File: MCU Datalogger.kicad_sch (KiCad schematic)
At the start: 25 parts, among them U1 24LC1025, U2 24LC1025, U3 DS1337S_, U4 ATMEGA328P-AU, Y1 16 MHz, Y2 32.768 KHz

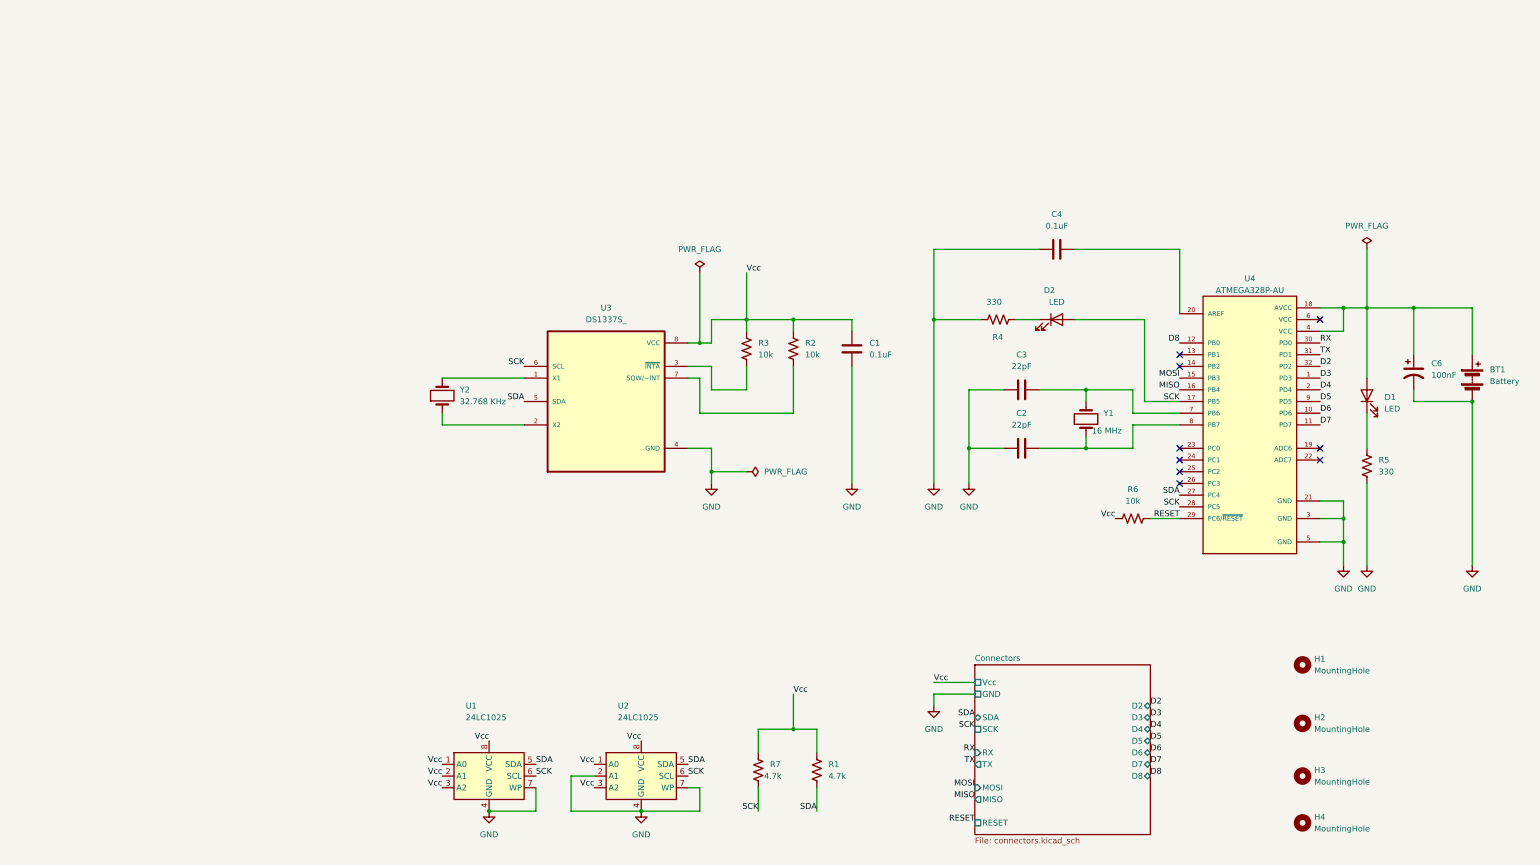
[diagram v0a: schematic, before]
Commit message: Completed comments and organization in schematic.
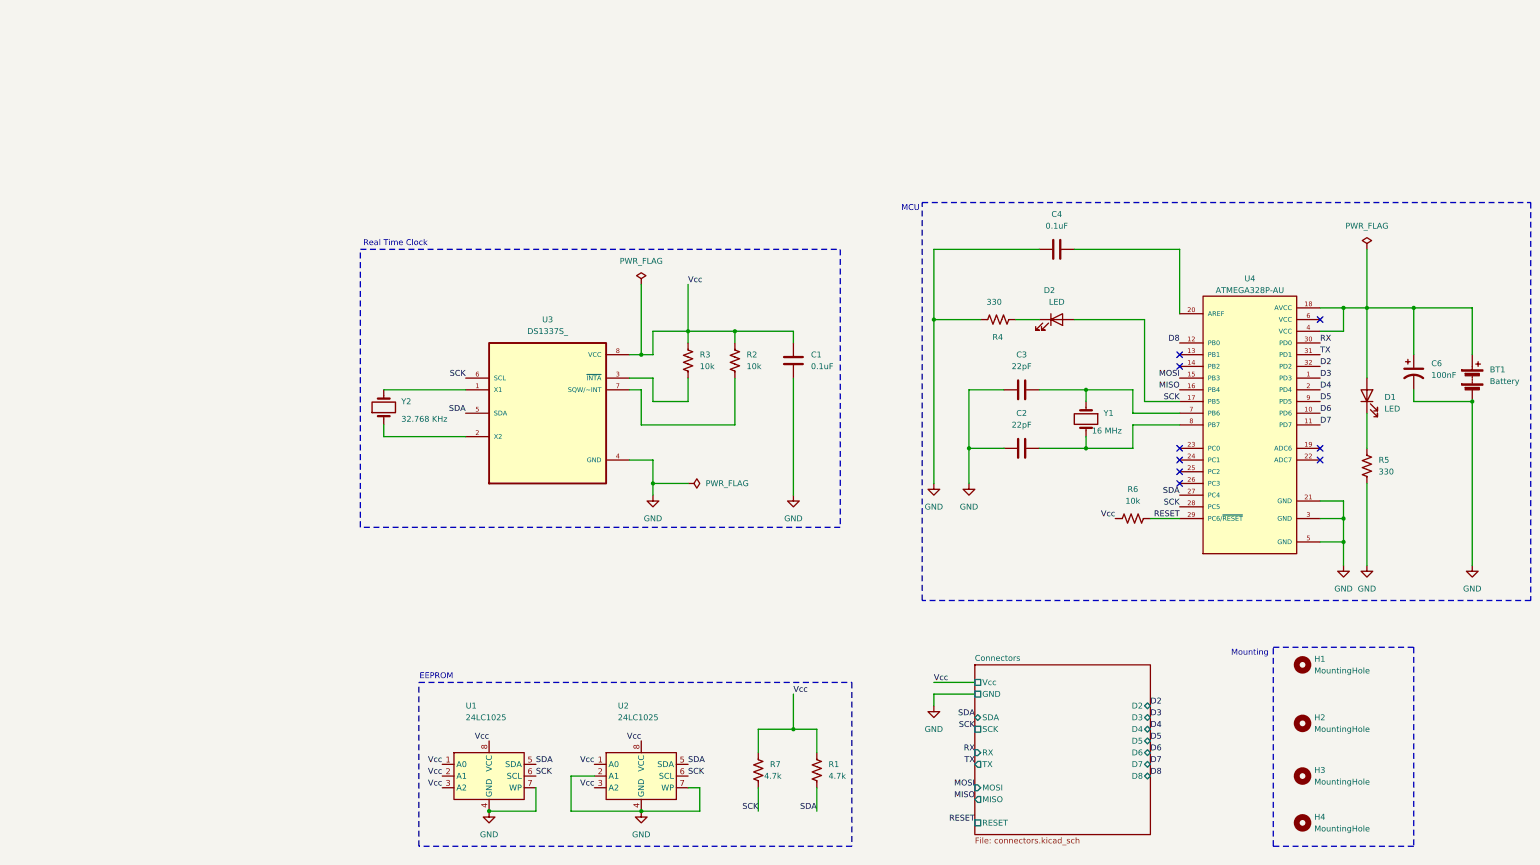
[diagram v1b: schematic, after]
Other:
- note added: "EEPROM"
- note added: "MCU"
- note added: "Mounting"
- note added: "Real Time Clock"
- moved on the sheet: C1, R2, R3, U3, Y2

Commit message: Fixed outstanding issues and set Silkscreen.
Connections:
- net Vcc: now also BT1.1 (+), C6.1, D1.2 (A), U4.18 (AVCC), U4.4 (VCC)
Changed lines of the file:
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@@
 	(wire
 		(pts
-			(xy 243.84 25.4) (xy 243.84 38.1)
-		)
-		(stroke
-			(width 0)
-			(type default)
-		)
-	)
-	(wire
-		(pts
 			(xy 106.68 43.18) (xy 106.68 45.72)
 		)
@@
 		)
 	)
+	(label "Vcc"
+		(at 243.84 38.1 0)
+		(fields_autoplaced yes)
+		(effects
+			(font
+				(size 1.27 1.27)
+			)
+			(justify left bottom)
+		)
+	)
 	(label "SDA"
 		(at 158.75 127 180)
@@
 					(unit 1)
 				)
-			)
-		)
-	)
-	(symbol
-		(lib_id "power:PWR_FLAG")
-		(at 243.84 25.4 0)
-		(unit 1)
-		(exclude_from_sim no)
-		(in_bom yes)
-		(on_board yes)
-		(dnp no)
-		(fields_autoplaced yes)
-		(property "Reference" "#FLG01"
-			(at 243.84 23.495 0)
-			(effects
-				(font
-					(size 1.27 1.27)
-				)
-				(hide yes)
-			)
-		)
-		(property "Value" "PWR_FLAG"
-			(at 243.84 20.32 0)
-			(effects
-				(font
-					(size 1.27 1.27)
-				)
-			)
-		)
-		(property "Footprint" ""
-			(at 243.84 25.4 0)
-			(effects
-				(font
-					(size 1.27 1.27)
-				)
-				(hide yes)
-			)
-		)
-		(property "Datasheet" "~"
-			(at 243.84 25.4 0)
-			(effects
-				(font
-					(size 1.27 1.27)
-				)
-				(hide yes)
-			)
-		)
-		(property "Description" "Special symbol for telling ERC where power comes from"
-			(at 243.84 25.4 0)
-			(effects
-				(font
-					(size 1.27 1.27)
-				)
-				(hide yes)
-			)
-		)
-		(pin "1"
-		)
-		(instances
-			(project ""
-				(path "/9701ff14-9a8f-43ab-a327-0923973e2750"
-					(reference "#FLG01")
-					(unit 1)
-				)

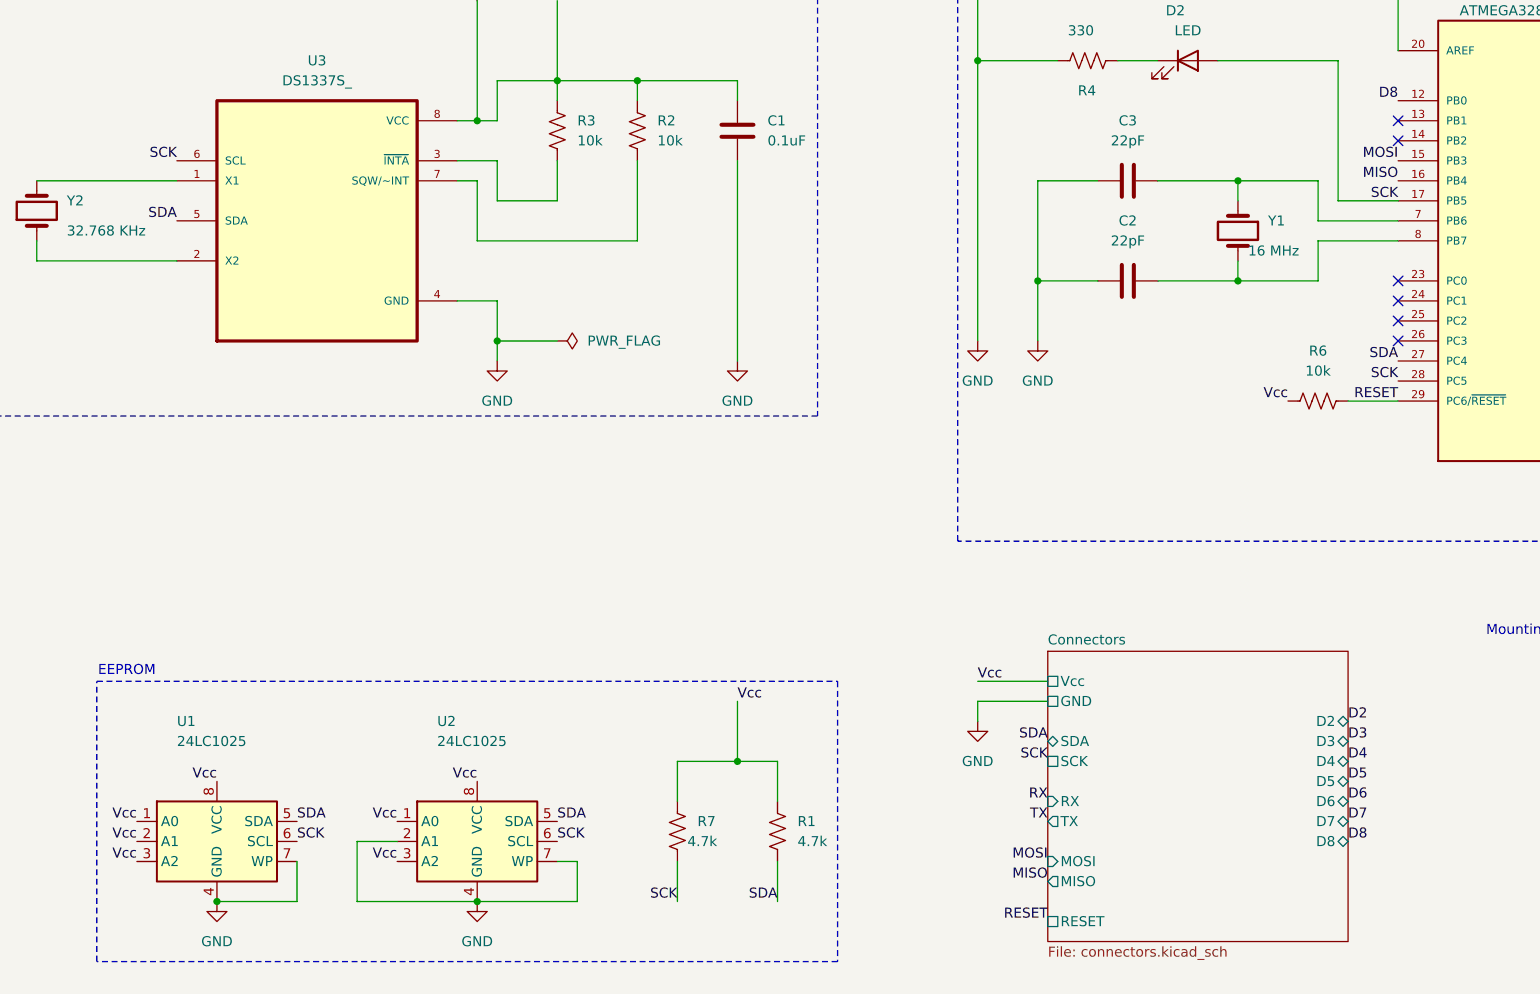
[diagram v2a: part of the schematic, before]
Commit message: Fixed defects relating to SCL/SCK confusion.
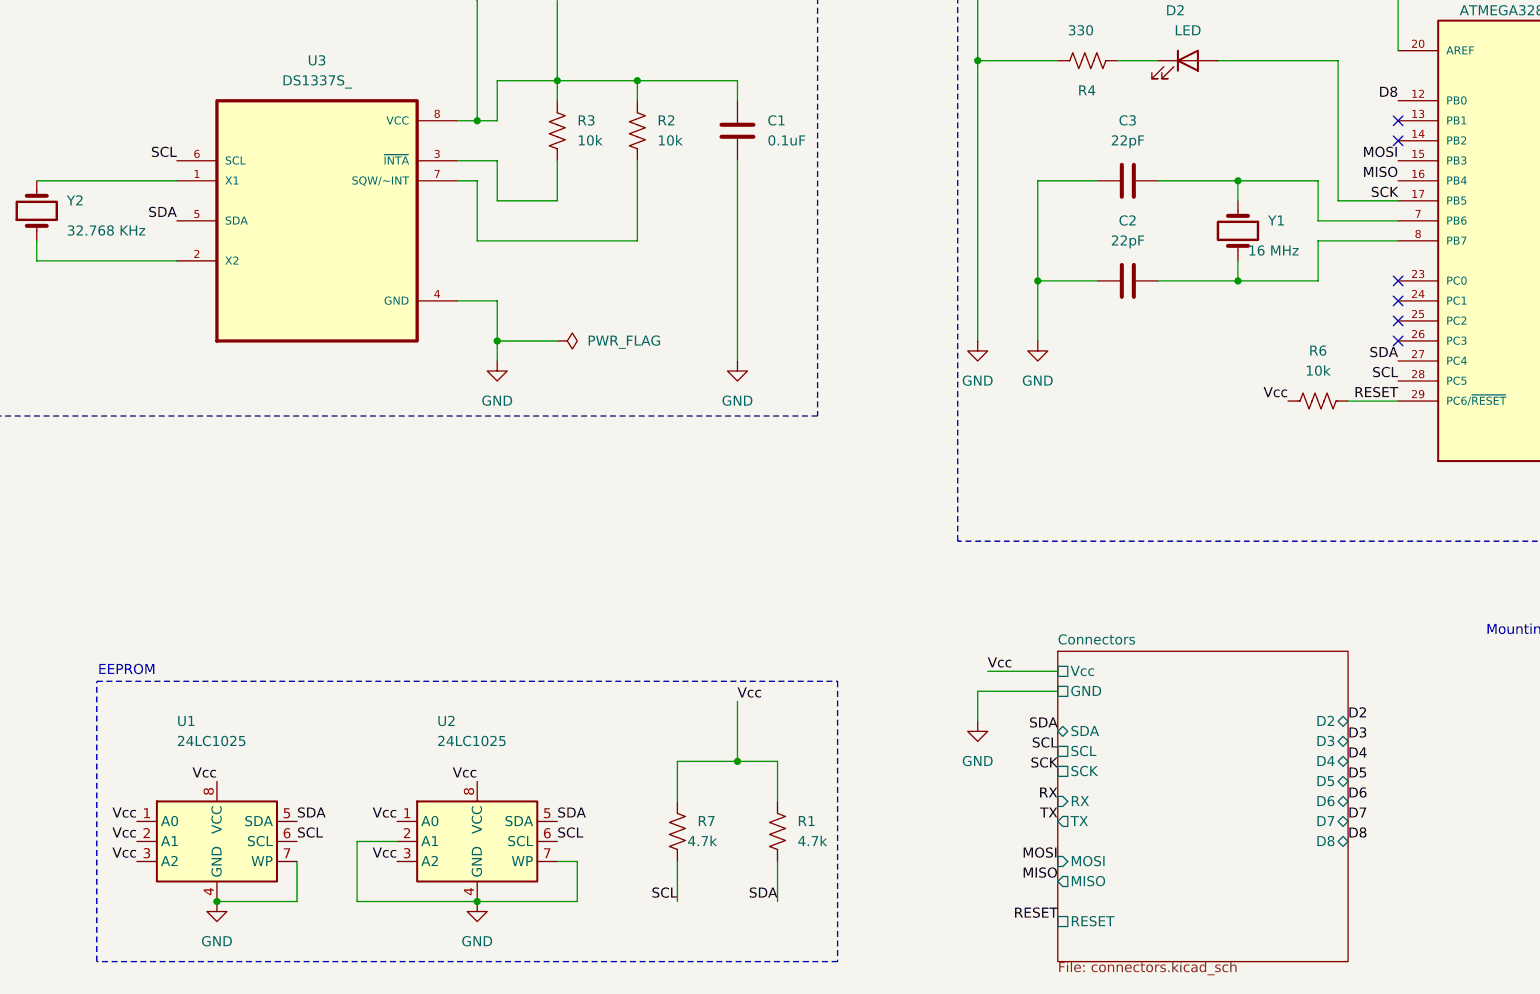
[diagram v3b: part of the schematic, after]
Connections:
- net SCK: no longer R7.1, U1.6 (SCL), U2.6 (SCL), U3.6 (SCL), U4.28 (PC5)
- new net SCL: R7.1, U1.6 (SCL), U2.6 (SCL), U3.6 (SCL), U4.28 (PC5)
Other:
- sheet Connectors ports: added SCL; removed none
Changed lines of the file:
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@@
 	(wire
 		(pts
+			(xy 149.86 120.65) (xy 160.02 120.65)
+		)
+		(stroke
+			(width 0)
+			(type default)
+		)
+	)
+	(wire
+		(pts
 			(xy 254 55.88) (xy 254 58.42)
 		)
@@
 	(wire
 		(pts
-			(xy 149.86 119.38) (xy 158.75 119.38)
-		)
-		(stroke
-			(width 0)
-			(type default)
-		)
-	)
-	(wire
-		(pts
-			(xy 158.75 121.92) (xy 149.86 121.92)
+			(xy 151.13 118.11) (xy 160.02 118.11)
 		)
 		(stroke
@@
 	(wire
 		(pts
-			(xy 149.86 121.92) (xy 149.86 124.46)
+			(xy 149.86 120.65) (xy 149.86 124.46)
 		)
 		(stroke
@@
 		)
 	)
-	(label "SCK"
+	(label "SCL"
 		(at 111.76 147.32 180)
 		(fields_autoplaced yes)
@@
 	)
 	(label "MOSI"
-		(at 158.75 142.24 180)
+		(at 160.02 142.24 180)
 		(fields_autoplaced yes)
 		(effects
@@
 		)
 	)
-	(label "SCK"
+	(label "SCL"
 		(at 63.5 139.7 0)
 		(fields_autoplaced yes)
@@
 		)
 	)
-	(label "SCK"
-		(at 158.75 129.54 180)
+	(label "SCL"
+		(at 160.02 128.27 180)
 		(fields_autoplaced yes)
 		(effects
@@
 	)
 	(label "RX"
-		(at 158.75 134.62 180)
+		(at 160.02 134.62 180)
 		(fields_autoplaced yes)
 		(effects
@@
 	)
 	(label "SDA"
-		(at 158.75 127 180)
+		(at 160.02 125.73 180)
+		(fields_autoplaced yes)
+		(effects
+			(font
+				(size 1.27 1.27)
+			)
+			(justify right bottom)
+		)
+	)
+	(label "SCK"
+		(at 160.02 130.81 180)
 		(fields_autoplaced yes)
 		(effects
@@
 	)
 	(label "Vcc"
-		(at 149.86 119.38 0)
+		(at 151.13 118.11 0)
 		(fields_autoplaced yes)
 		(effects
@@
 	)
 	(label "MISO"
-		(at 158.75 144.78 180)
+		(at 160.02 144.78 180)
 		(fields_autoplaced yes)
 		(effects
@@
 		)
 	)
-	(label "SCK"
+	(label "SCL"
 		(at 203.2 81.28 180)
 		(fields_autoplaced yes)
@@
 		)
 	)
-	(label "SCK"
+	(label "SCL"
 		(at 96.52 139.7 0)
 		(fields_autoplaced yes)
@@
 	)
 	(label "RESET"
-		(at 158.75 149.86 180)
+		(at 160.02 149.86 180)
 		(fields_autoplaced yes)
 		(effects
@@
 	)
 	(label "TX"
-		(at 158.75 137.16 180)
+		(at 160.02 137.16 180)
 		(fields_autoplaced yes)
 		(effects
@@
 		)
 	)
-	(label "SCK"
+	(label "SCL"
 		(at 48.26 53.34 180)
 		(fields_autoplaced yes)
@@
 	)
 	(sheet
-		(at 158.75 115.57)
-		(size 38.1 36.83)
-		(fields_autoplaced yes)
+		(at 160.02 115.57)
+		(size 36.83 39.37)
 		(stroke
 			(width 0.1524)
@@
 		)
 		(property "Sheetname" "Connectors"
-			(at 158.75 114.8584 0)
+			(at 160.02 114.8584 0)
 			(effects
 				(font
@@
 		)
 		(property "Sheetfile" "connectors.kicad_sch"
-			(at 158.75 152.9846 0)
+			(at 160.02 154.94 0)
 			(effects
 				(font
@@
 		)
 		(pin "SDA" bidirectional
-			(at 158.75 127 180)
+			(at 160.02 125.73 180)
 			(effects
 				(font
@@
 		)
 		(pin "Vcc" passive
-			(at 158.75 119.38 180)
+			(at 160.02 118.11 180)
 			(effects
 				(font
@@
 		)
 		(pin "GND" passive
-			(at 158.75 121.92 180)
-			(effects
-				(font
-					(size 1.27 1.27)
-				)
-				(justify left)
-			)
-		)
-		(pin "SCK" passive
-			(at 158.75 129.54 180)
+			(at 160.02 120.65 180)
 			(effects
 				(font
@@
 		)
 		(pin "RX" input
-			(at 158.75 134.62 180)
+			(at 160.02 134.62 180)
 			(effects
 				(font
@@
 		)
 		(pin "TX" output
-			(at 158.75 137.16 180)
+			(at 160.02 137.16 180)
 			(effects
 				(font
@@
 		)
 		(pin "MOSI" input
-			(at 158.75 142.24 180)
+			(at 160.02 142.24 180)
 			(effects
 				(font
@@
 		)
 		(pin "MISO" output
-			(at 158.75 144.78 180)
+			(at 160.02 144.78 180)
 			(effects
 				(font
@@
 		)
 		(pin "RESET" passive
-			(at 158.75 149.86 180)
+			(at 160.02 149.86 180)
+			(effects
+				(font
+					(size 1.27 1.27)
+				)
+				(justify left)
+			)
+		)
+		(pin "SCL" passive
+			(at 160.02 128.27 180)
+			(effects
+				(font
+					(size 1.27 1.27)
+				)
+				(justify left)
+			)
+		)
+		(pin "SCK" passive
+			(at 160.02 130.81 180)
 			(effects
 				(font

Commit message: Random changes for experimentation.
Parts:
- added U5: MSC1212Y5PAGT, Footprints:QFP50P1200X1200X120-64N, symbol MSC1212Y5PAGT:MSC1212Y5PAGT
- R1, R2, R3, R4, R5, R6, R7: symbol Device:R_US -> Device:R
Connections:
- new net: U5.11 (DVDD), U5.14 (DVDD), U5.15 (DVDD), U5.42 (DVDD), U5.58 (DVDD)
- new net: U5.12 (DGND), U5.41 (DGND), U5.57 (DGND)

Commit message: Changed back some experiments.
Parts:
- removed U5: MSC1212Y5PAGT, Footprints:QFP50P1200X1200X120-64N, symbol MSC1212Y5PAGT:MSC1212Y5PAGT
- R1, R2, R3, R4, R5, R6, R7: symbol Device:R -> Device:R_US
